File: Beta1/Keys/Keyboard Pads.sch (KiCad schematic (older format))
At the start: 208 parts, among them U0 APA102C, U1 APA102C, U10 APA102C, U11 APA102C, U12 APA102C, U13 APA102C, U14 APA102C, U15 APA102C, U16 APA102C, U17 APA102C, U18 APA102C, U19 APA102C, U2 APA102C, U20 APA102C, U21 APA102C, U22 APA102C, U23 APA102C, U24 APA102C, U25 APA102C, U26 APA102C, U27 APA102C, U28 APA102C, U29 APA102C, U3 APA102C, U30 APA102C, U31 APA102C, U32 SN74LV1T125DBVR, U33 SN74LVC2T45DCTT, U4 APA102C, U5 APA102C, U6 APA102C, U7 APA102C, U8 APA102C, U9 APA102C

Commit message: Basic layout of synth
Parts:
- removed +5V_IN1, CLK0, CLK16, D0, D16, GND0: CONN_01X01, Liberry:single_0.1, symbol CONN_01X01
- removed C0, C1, C10, C11, C12, C13, C14, C15, C16, C17, C18, C19, C2, C20, C21, C22, C23, C24, C25, C26, C27, C28, C29, C3, C30, C31, C33, C34, C4, C5, C6, C7, C8, C9: 0.1u, Capacitors_SMD:C_0603, symbol C
- removed CLK1, CLK10, CLK11, CLK12, CLK13, CLK14, CLK15, CLK17, CLK18, CLK19, CLK2, CLK20, CLK21, CLK22, CLK23, CLK24, CLK25, CLK26, CLK27, CLK28, CLK29, CLK3, CLK30, CLK31, CLK4, CLK5, CLK6, CLK7, CLK8, CLK9, D1, D10, D11, D12, D13, D14, D15, D17, D18, D19, D2, D20, D21, D22, D23, D24, D25, D26, D27, D28, D29, D3, D30, D31, D4, D5, D6, D7, D8, D9: CONN_01X01, Liberry:TESTPAD, symbol CONN_01X01
- removed RC0, RC1, RC10, RC11, RC12, RC13, RC14, RC15, RC16, RC17, RC18, RC19, RC2, RC20, RC21, RC22, RC23, RC24, RC25, RC26, RC27, RC28, RC29, RC3, RC30, RC31, RC4, RC5, RC6, RC7, RC8, RC9, RD0, RD1, RD10, RD11, RD12, RD13, RD14, RD15, RD16, RD17, RD18, RD19, RD2, RD20, RD21, RD22, RD23, RD24, RD25, RD26, RD27, RD28, RD29, RD3, RD30, RD31, RD4, RD5, RD6, RD7, RD8, RD9: ZERO, Resistors_SMD:R_0603, symbol R
- removed U0, U1, U10, U11, U12, U13, U14, U15, U16, U17, U18, U19, U2, U20, U21, U22, U23, U24, U25, U26, U27, U28, U29, U3, U30, U31, U4, U5, U6, U7, U8, U9: APA102C, Liberry:PLCC6-1.6x4.2_LED, symbol APA102C
- removed U32: SN74LV1T125DBVR, Liberry:SOT23-5, symbol SN74LV1T125DBVR
- removed U33: SN74LVC2T45DCTT, Liberry:SSOP8, symbol SN74LVC2T45DCTT
- added PAD0, PAD1, PAD100, PAD101, PAD102, PAD103, PAD104, PAD105, PAD106, PAD107, PAD2, PAD3, PAD4, PAD5, PAD6, PAD7: TOUCHPAD_10CM, Liberry:TOUCH_PAD_10CM, symbol TOUCHPAD_10CM
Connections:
- net labels added: PAD0, PAD1, PAD100, PAD101, PAD102, PAD103, PAD104, PAD105, PAD106, PAD107, PAD2, PAD3, PAD4, PAD5, PAD6, PAD7
- net labels removed: +5V, CLK12, CLK16, CLK24, CLK32, CLK4, CLK8, D12, D16, D24, D32, D4, D8
- wire segments 566 -> 26
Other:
- moved on the sheet: CLK32, CLKOUT31, D32, DOUT31

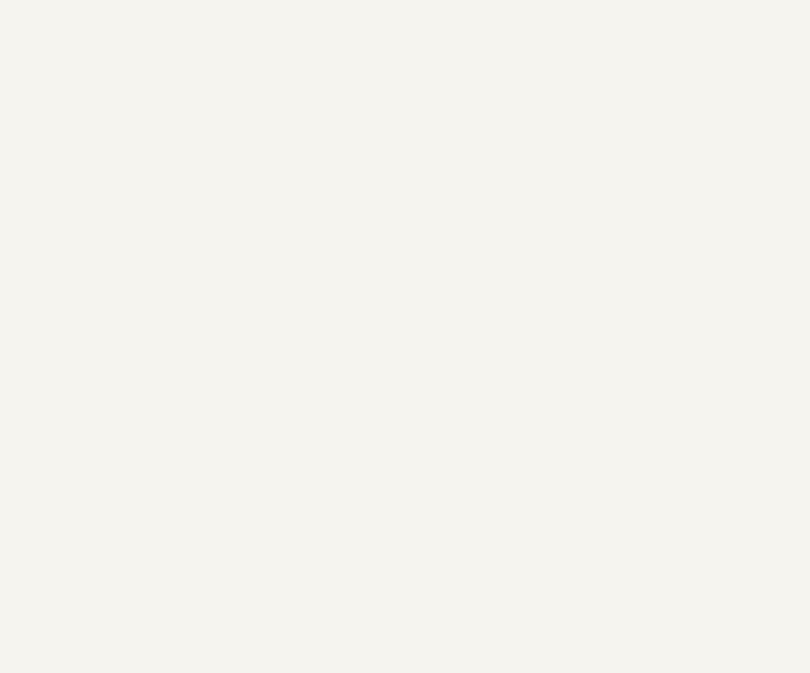
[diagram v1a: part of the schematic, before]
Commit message: Added 1 octave keyboard footprint and into pcb.
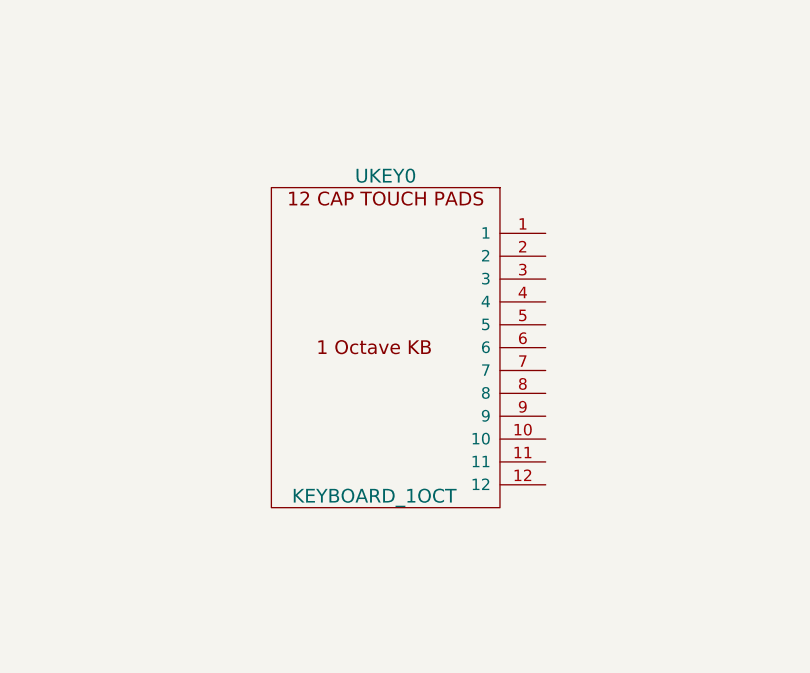
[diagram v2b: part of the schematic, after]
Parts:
- added UKEY0: KEYBOARD_1OCT, Liberry:Keyboard_1_Octave_20CM, symbol KEYBOARD_1OCT
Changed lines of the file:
@@
 $EndComp
 $Comp
-L +3.3V #PWR099
+L +3.3V #PWR01
 U 1 1 582EA21A
 P 4200 750
-F 0 "#PWR099" H 4200 600 50  0001 C CNN
+F 0 "#PWR01" H 4200 600 50  0001 C CNN
 F 1 "+3.3V" H 4200 890 50  0000 C CNN
 F 2 "" H 4200 750 50  0000 C CNN
@@
 $EndComp
 $Comp
-L GND #PWR0100
+L GND #PWR02
 U 1 1 582F5B3F
 P 4250 1300
-F 0 "#PWR0100" H 4250 1050 50  0001 C CNN
+F 0 "#PWR02" H 4250 1050 50  0001 C CNN
 F 1 "GND" H 4250 1150 50  0000 C CNN
 F 2 "" H 4250 1300 50  0000 C CNN
@@
 $EndComp
 $Comp
-L GND #PWR0101
+L GND #PWR03
 U 1 1 582FC796
 P 5700 3000
-F 0 "#PWR0101" H 5700 2750 50  0001 C CNN
+F 0 "#PWR03" H 5700 2750 50  0001 C CNN
 F 1 "GND" H 5700 2850 50  0000 C CNN
 F 2 "" H 5700 3000 50  0000 C CNN
@@
 $EndComp
 $Comp
-L +3.3V #PWR0102
+L +3.3V #PWR04
 U 1 1 582FCA14
 P 5700 2600
-F 0 "#PWR0102" H 5700 2450 50  0001 C CNN
+F 0 "#PWR04" H 5700 2450 50  0001 C CNN
 F 1 "+3.3V" H 5700 2740 50  0000 C CNN
 F 2 "" H 5700 2600 50  0000 C CNN
@@
 Text Label 9600 2900 0    60   ~ 0
 PAD107
+$Comp
+L KEYBOARD_1OCT UKEY0
+U 1 1 5830195A
+P 7850 4350
+F 0 "UKEY0" H 7150 4600 60  0000 C CNN
+F 1 "KEYBOARD_1OCT" H 7100 3200 60  0000 C CNN
+F 2 "Liberry:Keyboard_1_Octave_20CM" H 7850 3250 60  0001 C CNN
+F 3 "" H 7850 3250 60  0001 C CNN
+F 4 "PCB" H 7850 4350 60  0001 C CNN "MFG"
+F 5 "PCB" H 7850 4350 60  0001 C CNN "MPN"
+	1    7850 4350
+	1    0    0    -1
+$EndComp
 $EndSCHEMATC

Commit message: Add MPR
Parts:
- added U1: MPR121TH, Liberry:MPR121TH, symbol MPR121TH
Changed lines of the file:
@@
+	1    0    0    -1
+$EndComp
+$Comp
+L MPR121TH U1
+U 1 1 582FE9DC
+P 10700 3850
+F 0 "U1" H 11000 3900 60  0000 C CNN
+F 1 "MPR121TH" H 10950 1600 60  0000 C CNN
+F 2 "Liberry:MPR121TH" H 10500 2850 60  0001 C CNN
+F 3 "" H 10500 2850 60  0001 C CNN
+F 4 "Believotron" H 10700 3850 60  0001 C CNN "MFG"
+F 5 "BTWLMPR121TH" H 10700 3850 60  0001 C CNN "MPN"
+	1    10700 3850
 	1    0    0    -1
 $EndComp

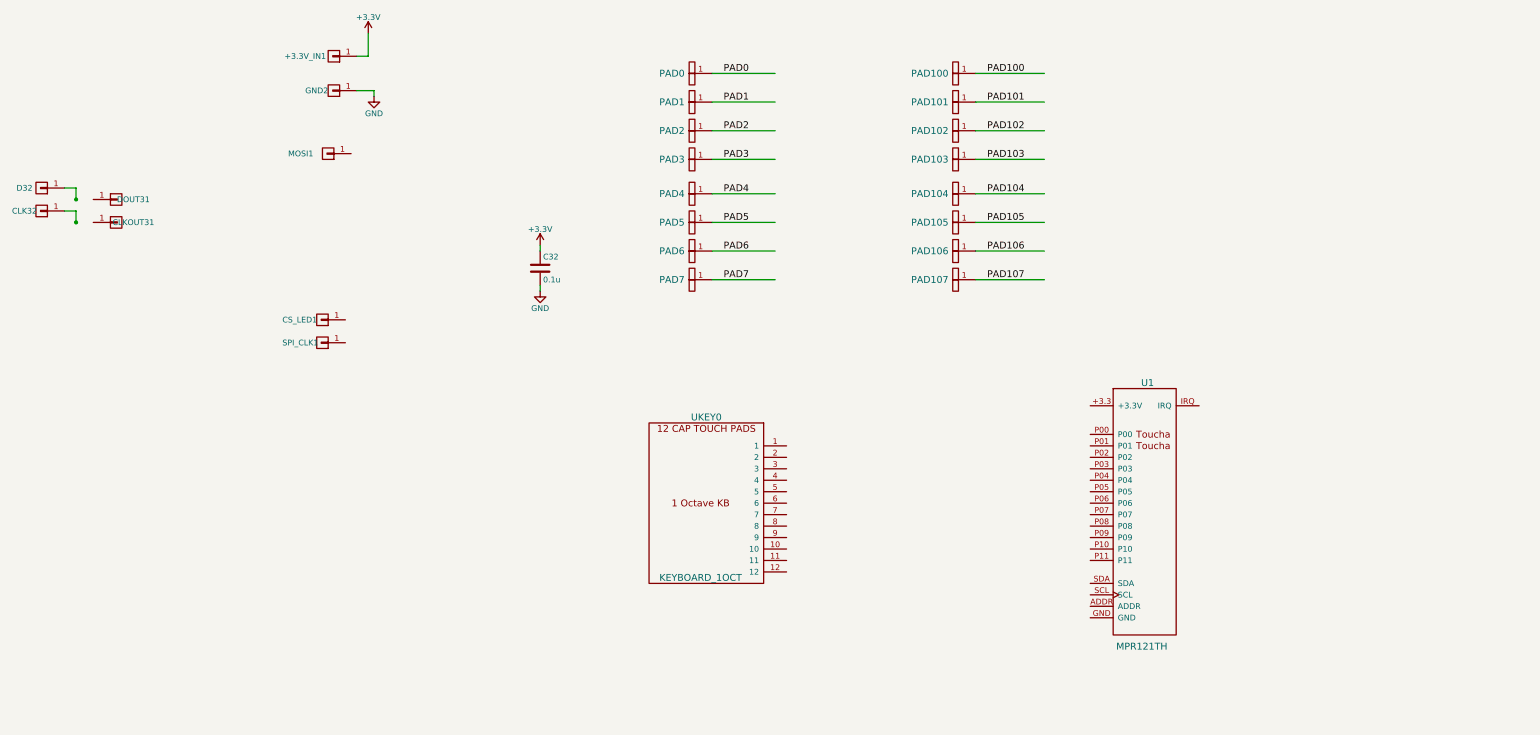
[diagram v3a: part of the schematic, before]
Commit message: Finished placement and routing of 1/2 Height Keypads. Ready to export.
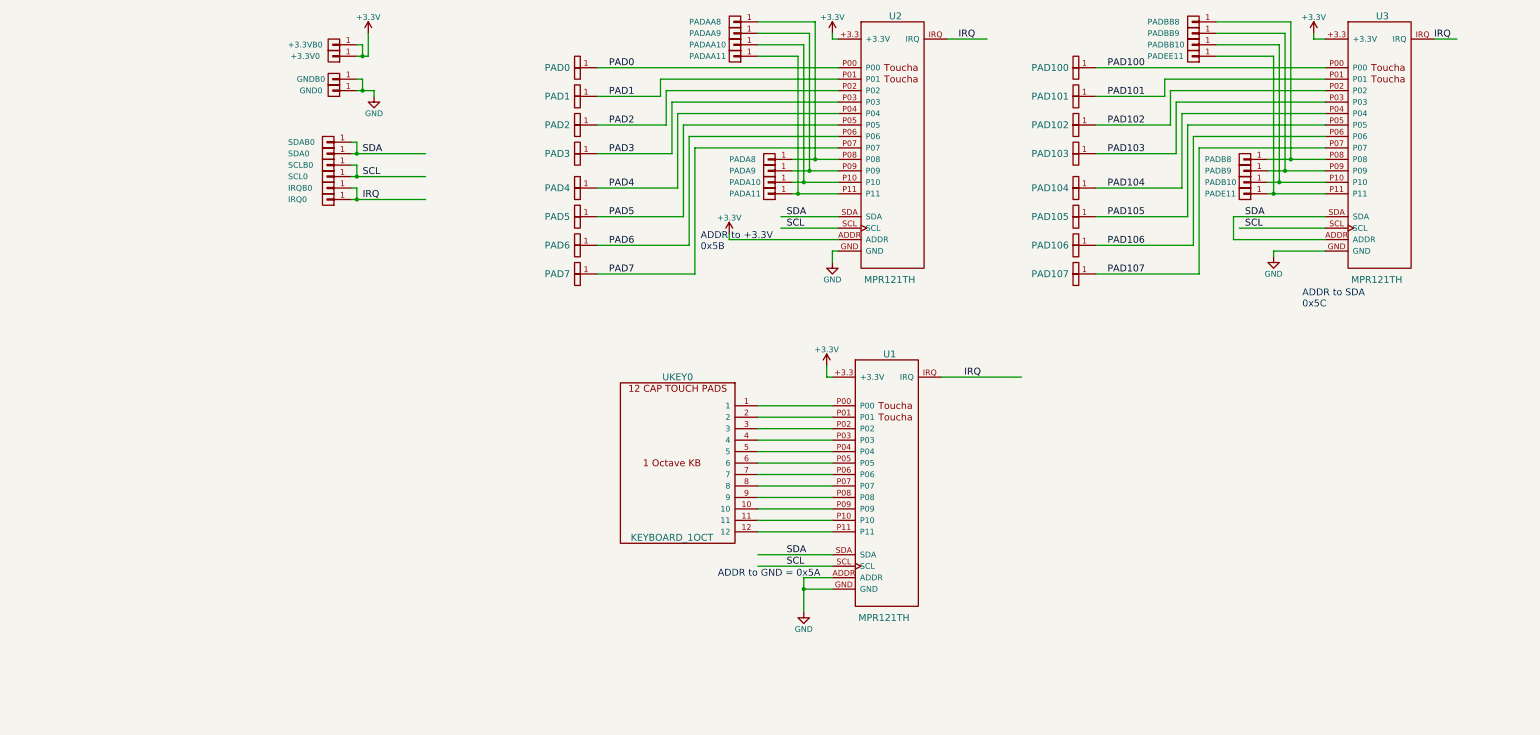
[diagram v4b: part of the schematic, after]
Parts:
- removed C32: 0.1u, Capacitors_SMD:C_0603, symbol C
- removed CLK32, D32: CONN_01X01, Liberry:TESTPAD, symbol CONN_01X01
- removed CLKOUT31, CS_LED1, DOUT31, SPI_CLK1: CONN_01X01, Liberry:single_0.1, symbol CONN_01X01
- added +3.3VB0, GNDB0, IRQ0, IRQB0, PADA10, PADA11, PADA8, PADA9, PADAA10, PADAA11, PADAA8, PADAA9, PADB10, PADB8, PADB9, PADBB10, PADBB8, PADBB9, PADE11, PADEE11, SCL0, SCLB0, SDAB0: CONN_01X01, Liberry:single_0.1, symbol CONN_01X01
- added U2, U3: MPR121TH, Liberry:MPR121TH, symbol MPR121TH
- renumbered +3.3V_IN1 to +3.3V0, GND2 to GND0, MOSI1 to SDA0
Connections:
- net labels added: IRQ, SCL, SDA
- wire segments 26 -> 123
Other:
- note added: "ADDR to +3.3V\n0x5B\n"
- note added: "ADDR to GND = 0x5A"
- note added: "ADDR to SDA\n0x5C"
- moved on the sheet: PAD0, PAD1, PAD100, PAD101, PAD102, PAD103, PAD104, PAD105, PAD106, PAD107, PAD2, PAD3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

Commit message: Minor Fuss. Apologies.
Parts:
- removed PADA10, PADA11, PADA8, PADA9, PADAA10, PADAA11, PADAA8, PADAA9, PADB10, PADB8, PADB9, PADBB10, PADBB8, PADBB9, PADE11, PADEE11: CONN_01X01, Liberry:single_0.1, symbol CONN_01X01
- removed U1, U2, U3: MPR121TH, Liberry:MPR121TH, symbol MPR121TH
- added +3.3VB0, +3.3VC0, GNDB0, GNDC0, IRQB0, IRQC0, SCLB0, SCLC0, SDAB0, SDAC0: CONN_01X01, Liberry:single_0.1, symbol CONN_01X01
- added U1, U2, U3: MPR121OTS, Liberry:MPR121OTS, symbol MPR121OTS
- renumbered +3.3VB0 to +3.3V0, +3.3V0 to +3.3VA0, GNDB0 to GNDA0, IRQB0 to IRQA0, SCLB0 to SCLA0, SDAB0 to SDAA0
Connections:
- net labels removed: PAD100, PAD101, PAD102, PAD103, PAD104, PAD105, PAD106, PAD107
- wire segments 123 -> 89
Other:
- note removed: "ADDR to +3.3V\n0x5B\n"
- note removed: "ADDR to GND = 0x5A"
- note removed: "ADDR to SDA\n0x5C"
- moved on the sheet: GND0, GNDA0, IRQ0, IRQA0, SCL0, SCLA0, SDA0, SDAA0
